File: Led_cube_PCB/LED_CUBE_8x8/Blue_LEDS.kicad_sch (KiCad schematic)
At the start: 34 parts, among them IC13 74AHCT244PW,118, IC14 74AHCT244PW,118, IC15 74AHCT244PW,118, IC17 74AHCT244PW,118, IC18 74AHCT244PW,118, IC23 74AHCT244PW,118, IC24 74AHCT244PW,118, IC25 74AHCT244PW,118, IC27 74AHC138PW,118

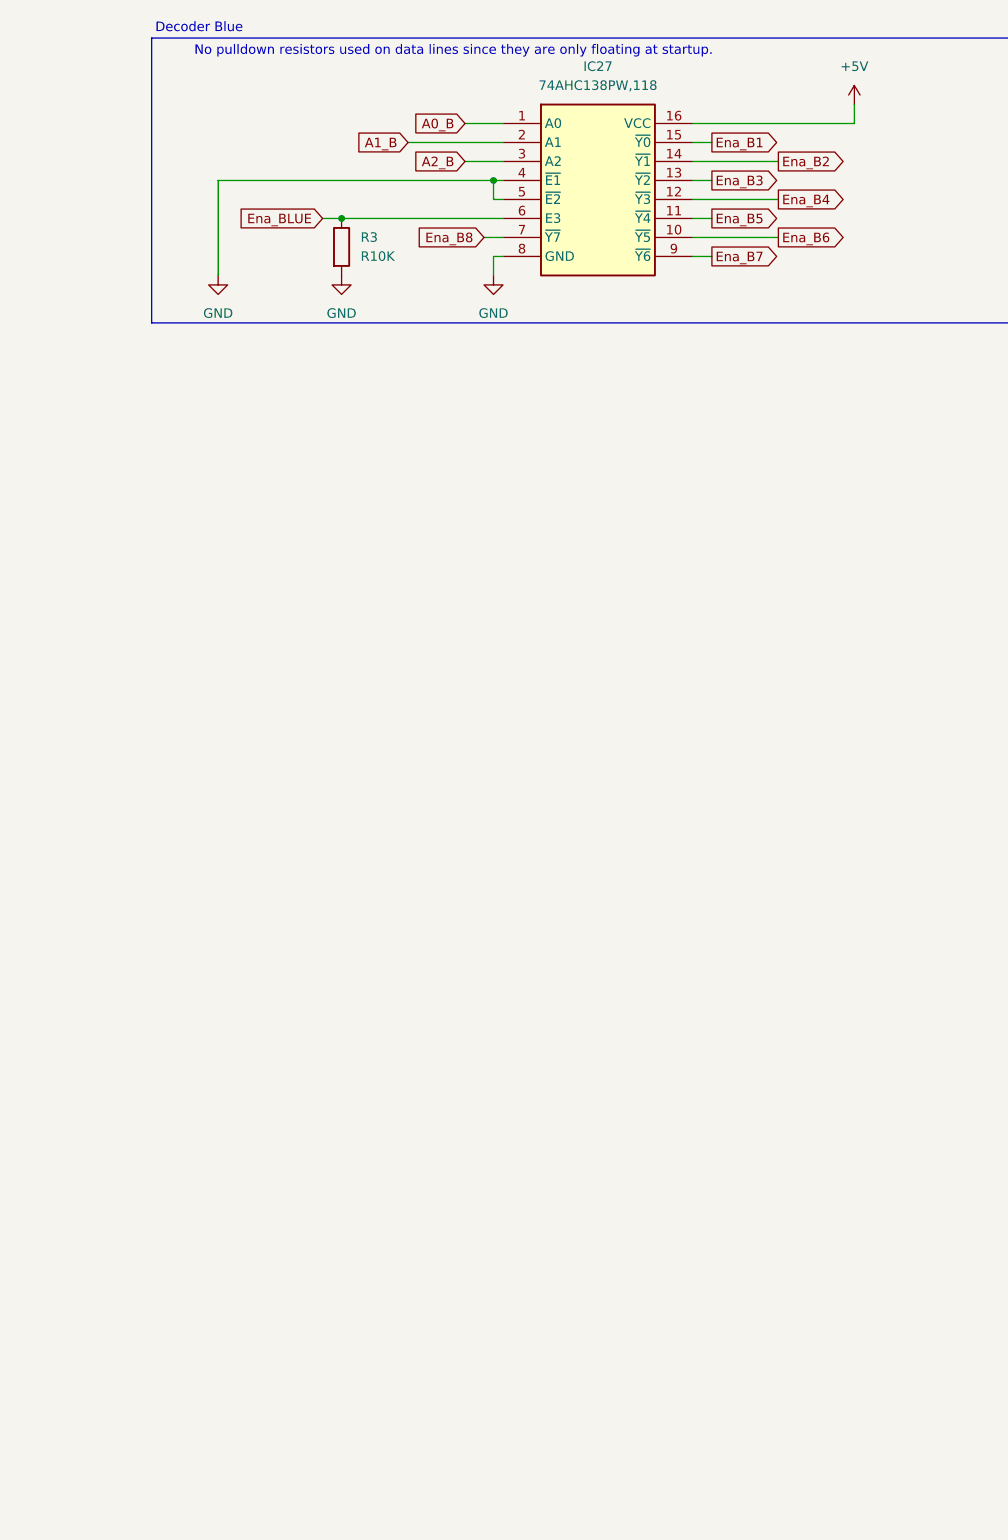
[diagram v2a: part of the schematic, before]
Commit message: added spice simulations folder, For simulating transients effect on the power buck converter. Also finished layer select in eeschema.
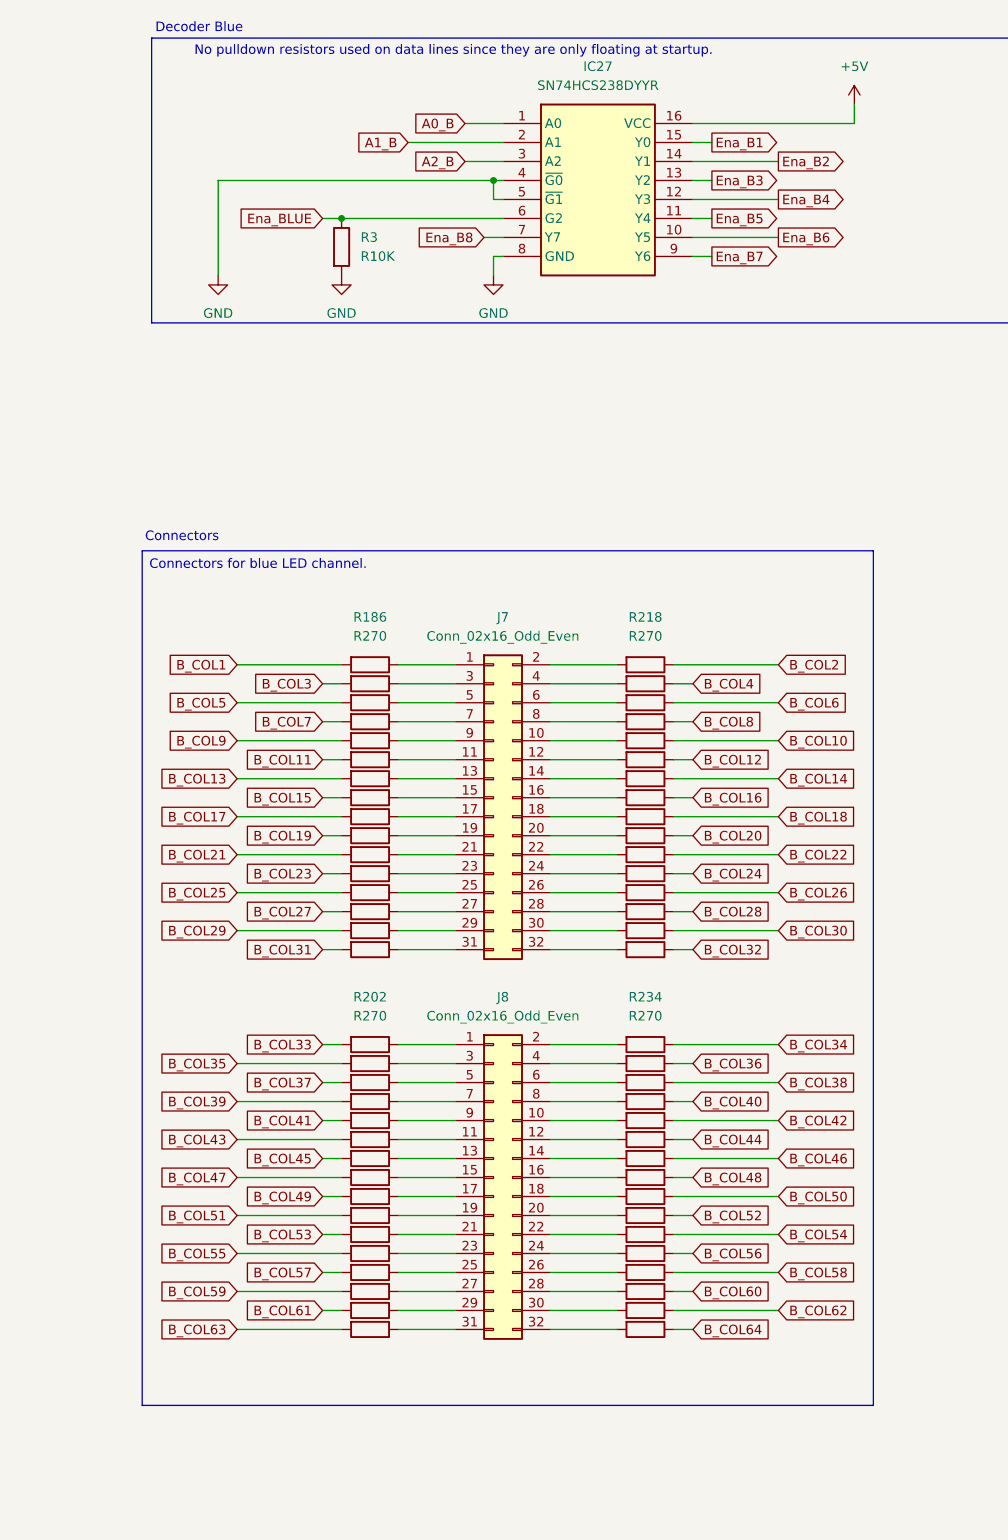
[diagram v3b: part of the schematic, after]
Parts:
- removed IC27: 74AHC138PW,118, SOP65P640X110-16N, symbol SamacSys_Parts:74AHC138PW,118
- added IC27: SN74HCS238DYYR, SOP50P326X110-16N, symbol SamacSys_Parts:SN74HCS238DYYR
- added J7, J8: Conn_02x16_Odd_Even, Connector_PinHeader_1.00mm:PinHeader_2x16_P1.00mm_Vertical, symbol Connector_Generic:Conn_02x16_Odd_Even
- added R186, R187, R188, R189, R190, R191, R192, R193, R194, R195, R196, R197, R198, R199, R200, R201, R202, R203, R204, R205, R206, R207, R208, R209, R210, R211, R212, R213, R214, R215, R216, R217, R218, R219, R220, R221, R222, R223, R224, R225, R226, R227, R228, R229, R230, R231, R232, R233, R234, R235, R236, R237, R238, R239, R240, R241, R242, R243, R244, R245, R246, R247, R248, R249: R270, symbol Device:R
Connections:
- net +5V: now also IC27.16 (VCC)
- net A0_B: now also IC27.1 (A0)
- net A1_B: now also IC27.2 (A1)
- net A2_B: now also IC27.3 (A2)
- net B_COL1: now also R186.2
- net B_COL10: now also R222.1
- net B_COL11: now also R191.2
- net B_COL12: now also R223.1
- net B_COL13: now also R192.2
- net B_COL14: now also R224.1
- net B_COL15: now also R193.2
- net B_COL16: now also R225.1
- net B_COL17: now also R194.2
- net B_COL18: now also R226.1
- net B_COL19: now also R195.2
- net B_COL2: now also R218.1
- net B_COL20: now also R227.1
- net B_COL21: now also R196.2
- net B_COL22: now also R228.1
- net B_COL23: now also R197.2
- net B_COL24: now also R229.1
- net B_COL25: now also R198.2
- net B_COL26: now also R230.1
- net B_COL27: now also R199.2
- net B_COL28: now also R231.1
- net B_COL29: now also R200.2
- net B_COL3: now also R187.2
- net B_COL30: now also R232.1
- net B_COL31: now also R201.2
- net B_COL32: now also R233.1
- net B_COL33: now also R202.2
- net B_COL34: now also R234.1
- net B_COL35: now also R203.2
- net B_COL36: now also R235.1
- net B_COL37: now also R204.2
- net B_COL38: now also R236.1
- net B_COL39: now also R205.2
- net B_COL4: now also R219.1
- net B_COL40: now also R237.1
- net B_COL41: now also R206.2
- net B_COL42: now also R238.1
- net B_COL43: now also R207.2
- net B_COL44: now also R239.1
- net B_COL45: now also R208.2
- net B_COL46: now also R240.1
- net B_COL47: now also R209.2
- net B_COL48: now also R241.1
- net B_COL49: now also R210.2
- net B_COL5: now also R188.2
- net B_COL50: now also R242.1
- net B_COL51: now also R211.2
- net B_COL52: now also R243.1
- net B_COL53: now also R212.2
- net B_COL54: now also R244.1
- net B_COL55: now also R213.2
- net B_COL56: now also R245.1
- net B_COL57: now also R214.2
- net B_COL58: now also R246.1
- net B_COL59: now also R215.2
- net B_COL6: now also R220.1
- net B_COL60: now also R247.1
- net B_COL61: now also R216.2
- net B_COL62: now also R248.1
- net B_COL63: now also R217.2
- net B_COL64: now also R249.1
- net B_COL7: now also R189.2
- net B_COL8: now also R221.1
- net B_COL9: now also R190.2
- net Ena_B1: now also IC27.15 (Y0)
- net Ena_B2: now also IC27.14 (Y1)
- net Ena_B3: now also IC27.13 (Y2)
- net Ena_B4: now also IC27.12 (Y3)
- net Ena_B5: now also IC27.11 (Y4)
- net Ena_B6: now also IC27.10 (Y5)
- net Ena_B7: now also IC27.9 (Y6)
- net Ena_B8: now also IC27.7 (Y7)
- net Ena_BLUE: now also IC27.6 (G2)
- net GND: now also IC27.4 (~{G0}), IC27.5 (~{G1}), IC27.8 (GND)
- new net: J7.23 (Pin_23), R197.1
- new net: J8.15 (Pin_15), R209.1
- new net: J8.26 (Pin_26), R246.2
- new net: J7.19 (Pin_19), R195.1
- new net: J8.7 (Pin_7), R205.1
- new net: J8.31 (Pin_31), R217.1
- new net: J8.4 (Pin_4), R235.2
- new net: J8.30 (Pin_30), R248.2
- new net: J7.1 (Pin_1), R186.1
- new net: J7.10 (Pin_10), R222.2
- new net: J7.11 (Pin_11), R191.1
- new net: J7.12 (Pin_12), R223.2
- new net: J7.13 (Pin_13), R192.1
- new net: J7.14 (Pin_14), R224.2
- new net: J7.15 (Pin_15), R193.1
- new net: J7.16 (Pin_16), R225.2
- new net: J7.17 (Pin_17), R194.1
- new net: J7.18 (Pin_18), R226.2
- new net: J7.2 (Pin_2), R218.2
- new net: J7.20 (Pin_20), R227.2
- new net: J7.21 (Pin_21), R196.1
- new net: J7.22 (Pin_22), R228.2
- new net: J7.24 (Pin_24), R229.2
- new net: J7.25 (Pin_25), R198.1
- new net: J7.26 (Pin_26), R230.2
- new net: J7.27 (Pin_27), R199.1
- new net: J7.28 (Pin_28), R231.2
- new net: J7.29 (Pin_29), R200.1
- new net: J7.3 (Pin_3), R187.1
- new net: J7.30 (Pin_30), R232.2
- new net: J7.31 (Pin_31), R201.1
- new net: J7.32 (Pin_32), R233.2
- new net: J7.4 (Pin_4), R219.2
- new net: J7.5 (Pin_5), R188.1
- new net: J7.6 (Pin_6), R220.2
- new net: J7.7 (Pin_7), R189.1
- new net: J7.8 (Pin_8), R221.2
- new net: J7.9 (Pin_9), R190.1
- new net: J8.8 (Pin_8), R237.2
- new net: J8.10 (Pin_10), R238.2
- new net: J8.17 (Pin_17), R210.1
- new net: J8.18 (Pin_18), R242.2
- new net: J8.23 (Pin_23), R213.1
- new net: J8.12 (Pin_12), R239.2
- new net: J8.22 (Pin_22), R244.2
- new net: J8.6 (Pin_6), R236.2
- new net: J8.25 (Pin_25), R214.1
- new net: J8.14 (Pin_14), R240.2
- new net: J8.9 (Pin_9), R206.1
- new net: J8.16 (Pin_16), R241.2
- new net: J8.32 (Pin_32), R249.2
- new net: J8.1 (Pin_1), R202.1
- new net: J8.11 (Pin_11), R207.1
- new net: J8.24 (Pin_24), R245.2
- new net: J8.21 (Pin_21), R212.1
- new net: J8.13 (Pin_13), R208.1
- new net: J8.19 (Pin_19), R211.1
- new net: J8.2 (Pin_2), R234.2
- new net: J8.20 (Pin_20), R243.2
- new net: J8.27 (Pin_27), R215.1
- new net: J8.28 (Pin_28), R247.2
- new net: J8.29 (Pin_29), R216.1
- new net: J8.3 (Pin_3), R203.1
- new net: J8.5 (Pin_5), R204.1
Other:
- note added: "Connectors"
